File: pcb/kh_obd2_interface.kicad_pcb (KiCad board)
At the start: 2 copper layers, 60 x 50 mm, 68 parts, among them J1 OBD2, J2 CAN, J3 USB-C 2.0, J4 RTC_BAT, J5 TC2030, J6 Conn_01x03_Pin, M1 MountingHole_3.2mm_M3_Pad_Top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, Q201 CSD18540Q5B, Q301 2N3904, SW1 NRST, SW2 SW_SPDT, U1 STM32G0B1RET6, U201 LM74500-Q1, U202 TVS2700DRV, U3 TPSM33620S5QRDNRQ1, U301 TCAN3403-Q1, U302 74LVC1G07, U303 SN74LV1T34DBV, U304 TLIN2027-Q1, U4 LM1117-Q1-3.3

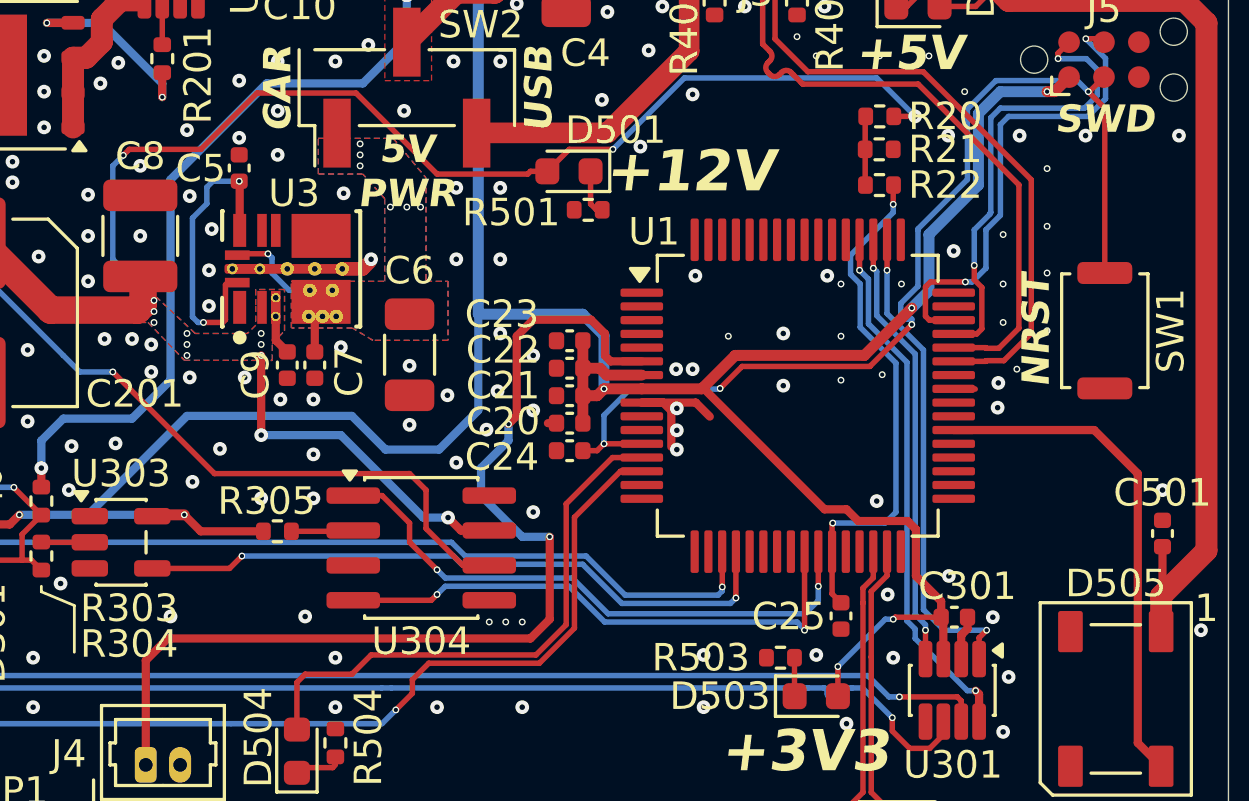
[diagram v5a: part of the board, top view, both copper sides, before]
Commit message: led dout testpoint
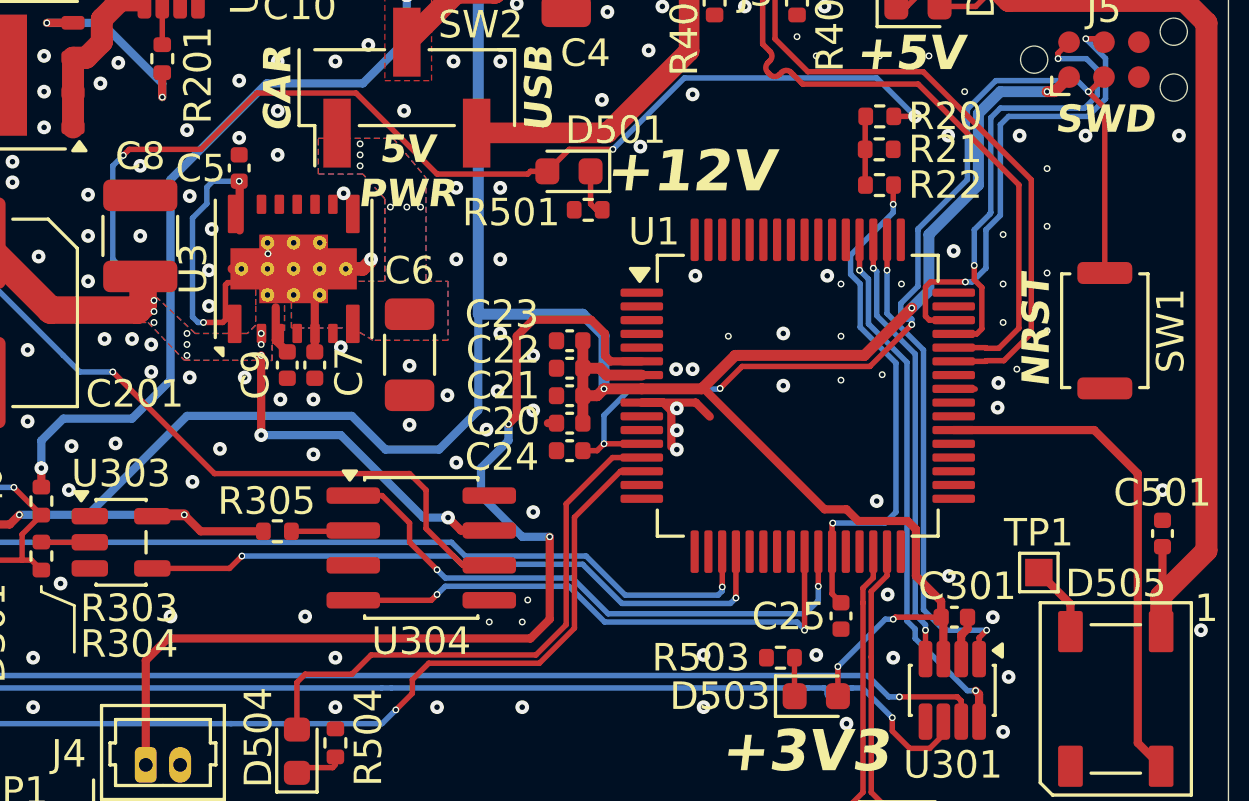
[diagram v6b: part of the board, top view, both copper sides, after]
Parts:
- added TP1: LED_DOUT, TestPoint:TestPoint_Pad_1.0x1.0mm, F.Cu at (70.6, 45.3)
- R305: value 5.1k -> 1k
- U3: footprint TIParts:RDN0011A-MFG -> Package_DFN_QFN:Texas_B3QFN-14-1EP_5x5.5mm_P0.65mm_ThermalVia
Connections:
- net /MCU/DISPLAY.DC renamed /MCU/MCU_DISPLAY.DC
- net /MCU/DISPLAY.RST renamed /MCU/MCU_DISPLAY.RST
- net /MCU/DISPLAY.SPI_CLK renamed /MCU/MCU_DISPLAY.SPI_CLK
- net /MCU/DISPLAY.SPI_CS renamed /MCU/MCU_DISPLAY.SPI_CS
- net /MCU/DISPLAY.SPI_MISO renamed /MCU/MCU_DISPLAY.SPI_MISO
- net /MCU/DISPLAY.SPI_MOSI renamed /MCU/MCU_DISPLAY.SPI_MOSI
- D505 pad 2: unconnected-(D505-DOUT-Pad2) -> Net-(D505-DOUT)
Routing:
- net Net-(D505-DOUT): track 0.00 -> 2.63 mm
- net GND: vias 195 -> 193
